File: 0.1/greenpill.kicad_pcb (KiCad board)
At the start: 4 copper layers, 17.4 x 53.1 mm, 31 parts, among them J1 Conn_01x20_Male, J2 Conn_01x20_Male, J3 Conn_01x04_Male, J5 USB_C_Receptacle_USB2.0, SW1 SW_Push, SW2 SW_Push, U1 ATSAMD51J18A-M, U2 MIC5504-3.3YM5, U3 S25FL064, Y1 Crystal_GND23

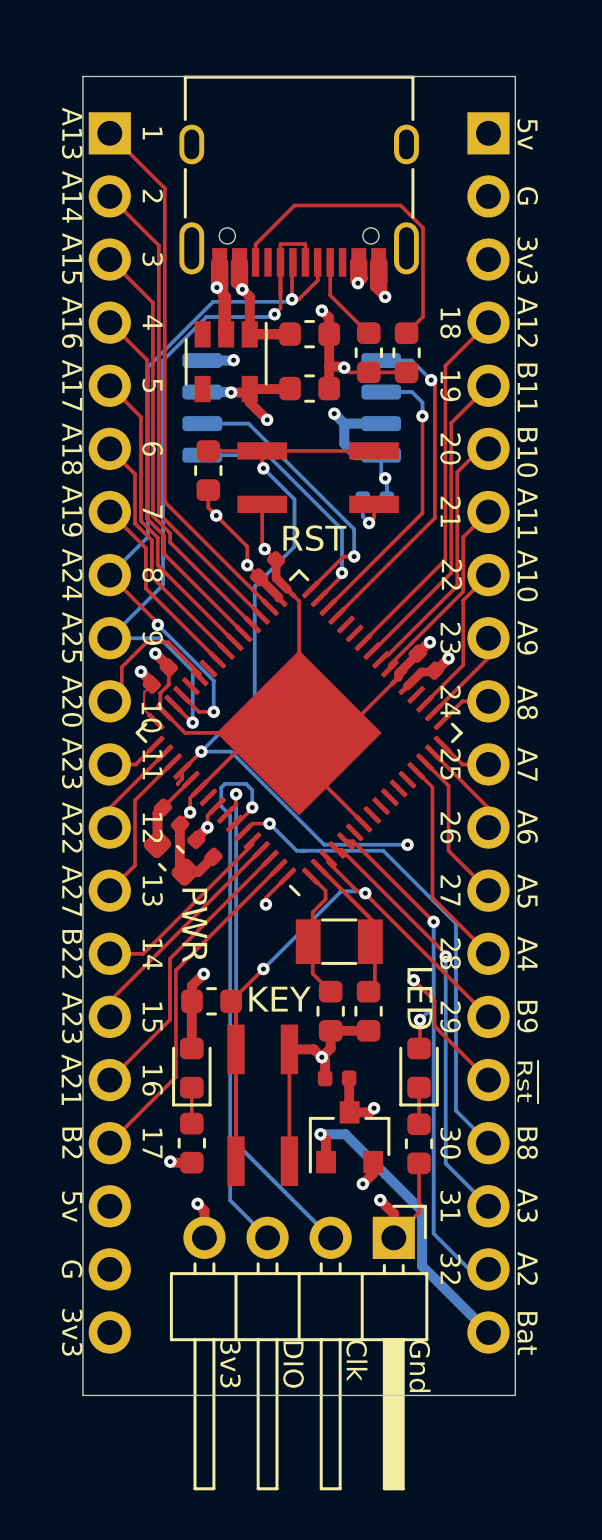
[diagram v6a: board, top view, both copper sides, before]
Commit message: Updated silkscreen
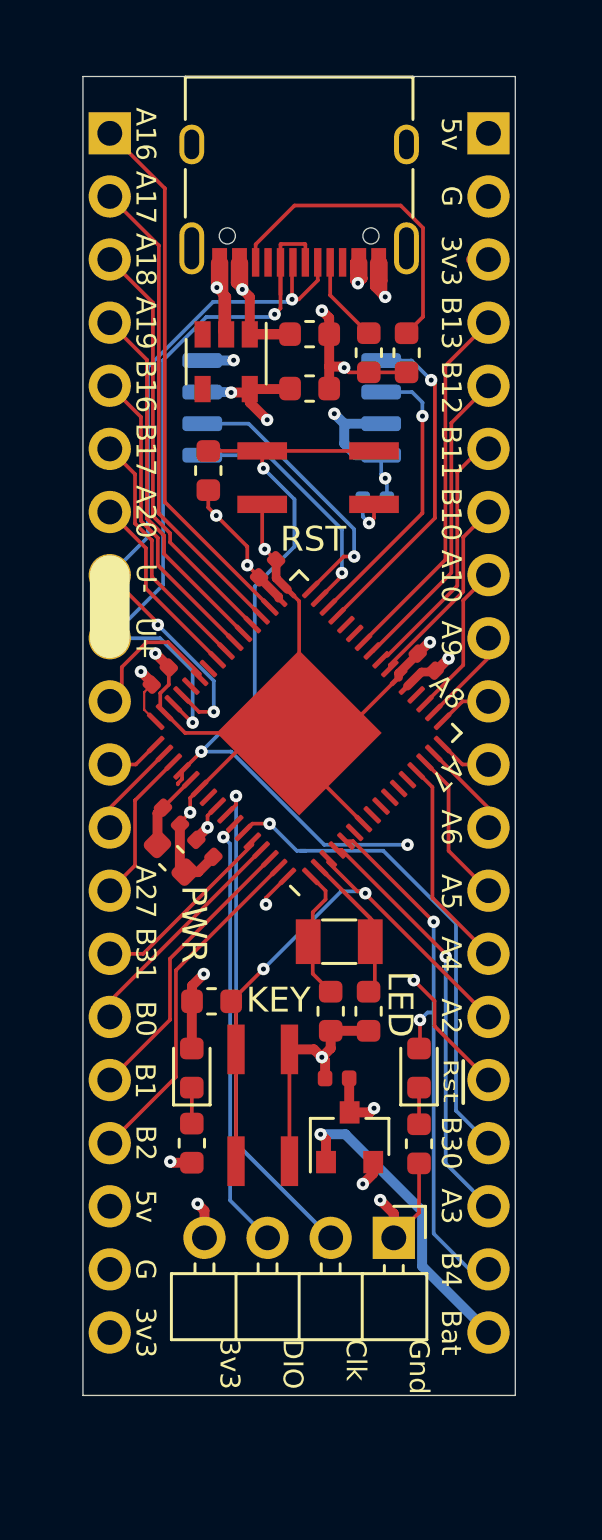
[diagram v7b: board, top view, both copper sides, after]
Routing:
- net /pa31: track 21.9 -> 17.6 mm
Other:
- board text added: "B0"
- board text added: "B1"
- board text added: "B12"
- board text added: "B13"
- board text added: "B16"
- board text added: "B17"
- board text added: "B23"
- board text added: "B30"
- board text added: "B31"
- board text added: "B4"
- board text added: "JLCJLCJLCJLC"
- board text added: "SPI flash"
- board text added: "U+"
- board text added: "U-"
- board text removed: "A11"
- board text removed: "A12"
- board text removed: "A13"
- board text removed: "A14"
- board text removed: "A15"
- board text removed: "A21"
- board text removed: "A23"
- board text removed: "A24"
- board text removed: "A25"
- board text removed: "B8"
- board text removed: "B9"

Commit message: poke layout a bit
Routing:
- net GND: track 75.2 -> 76.2 mm, vias 13 -> 14
- net /!reset: track 43.6 -> 42.9 mm
